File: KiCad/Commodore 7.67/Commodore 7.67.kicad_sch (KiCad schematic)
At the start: 22 parts, among them U1 SX1281IMLTRT, U2 SN65HVD74DR, U3 LPF-B0R3, Y1 52MHz

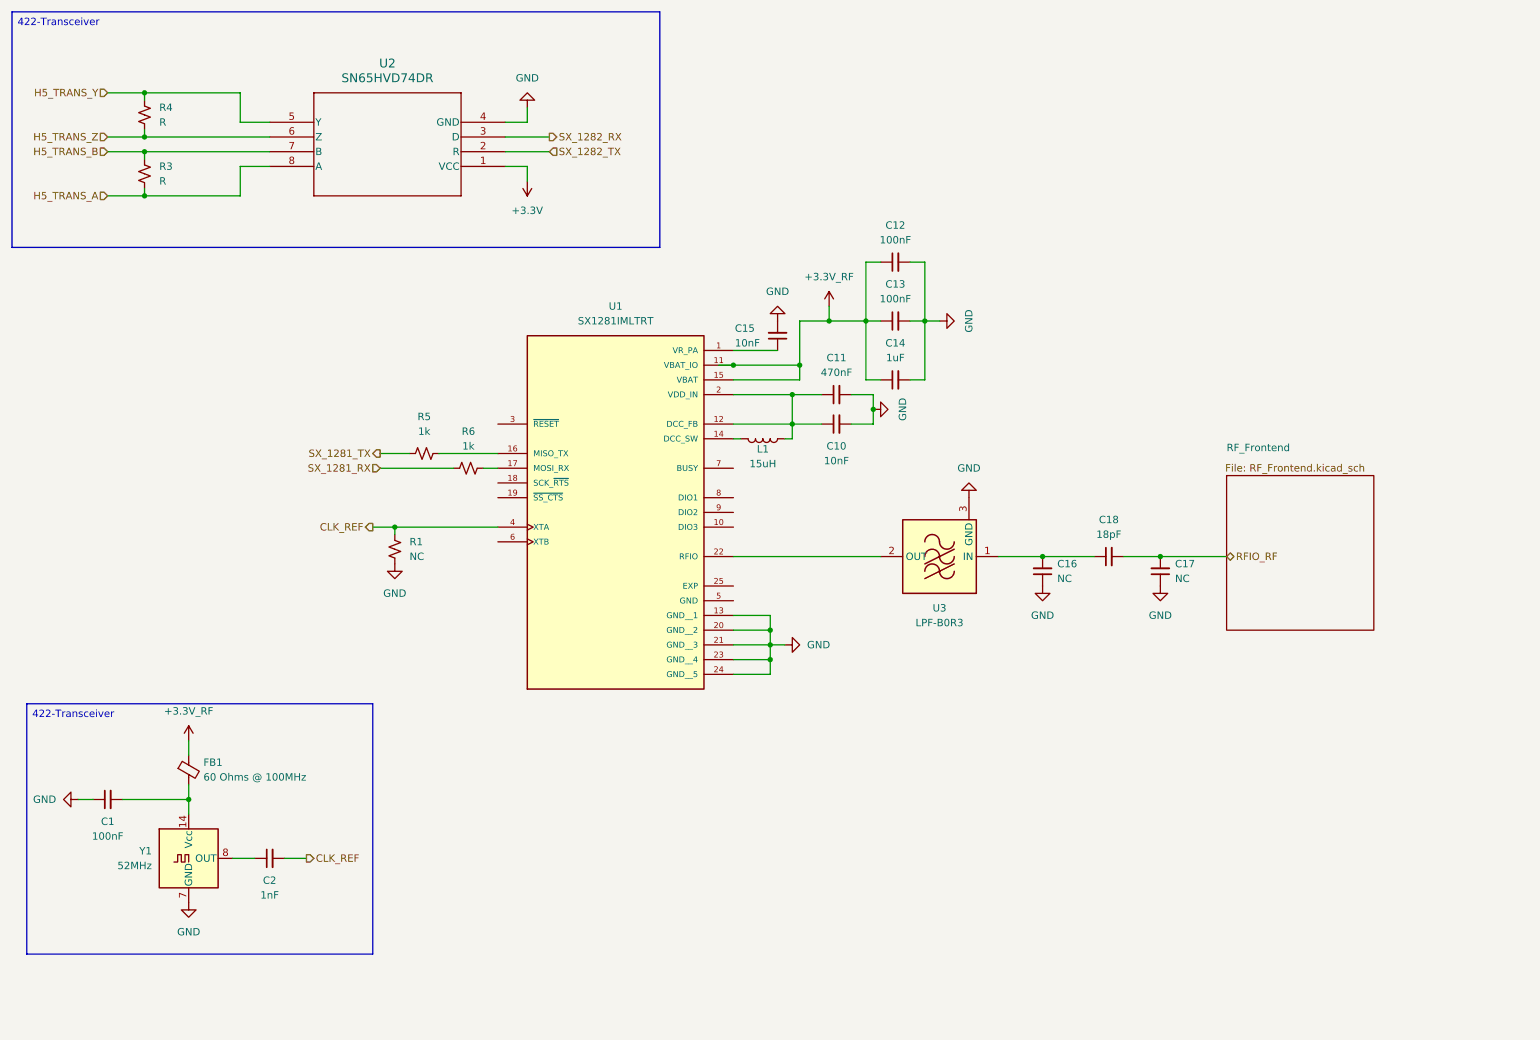
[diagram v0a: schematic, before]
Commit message: ts updates for ts sx1281
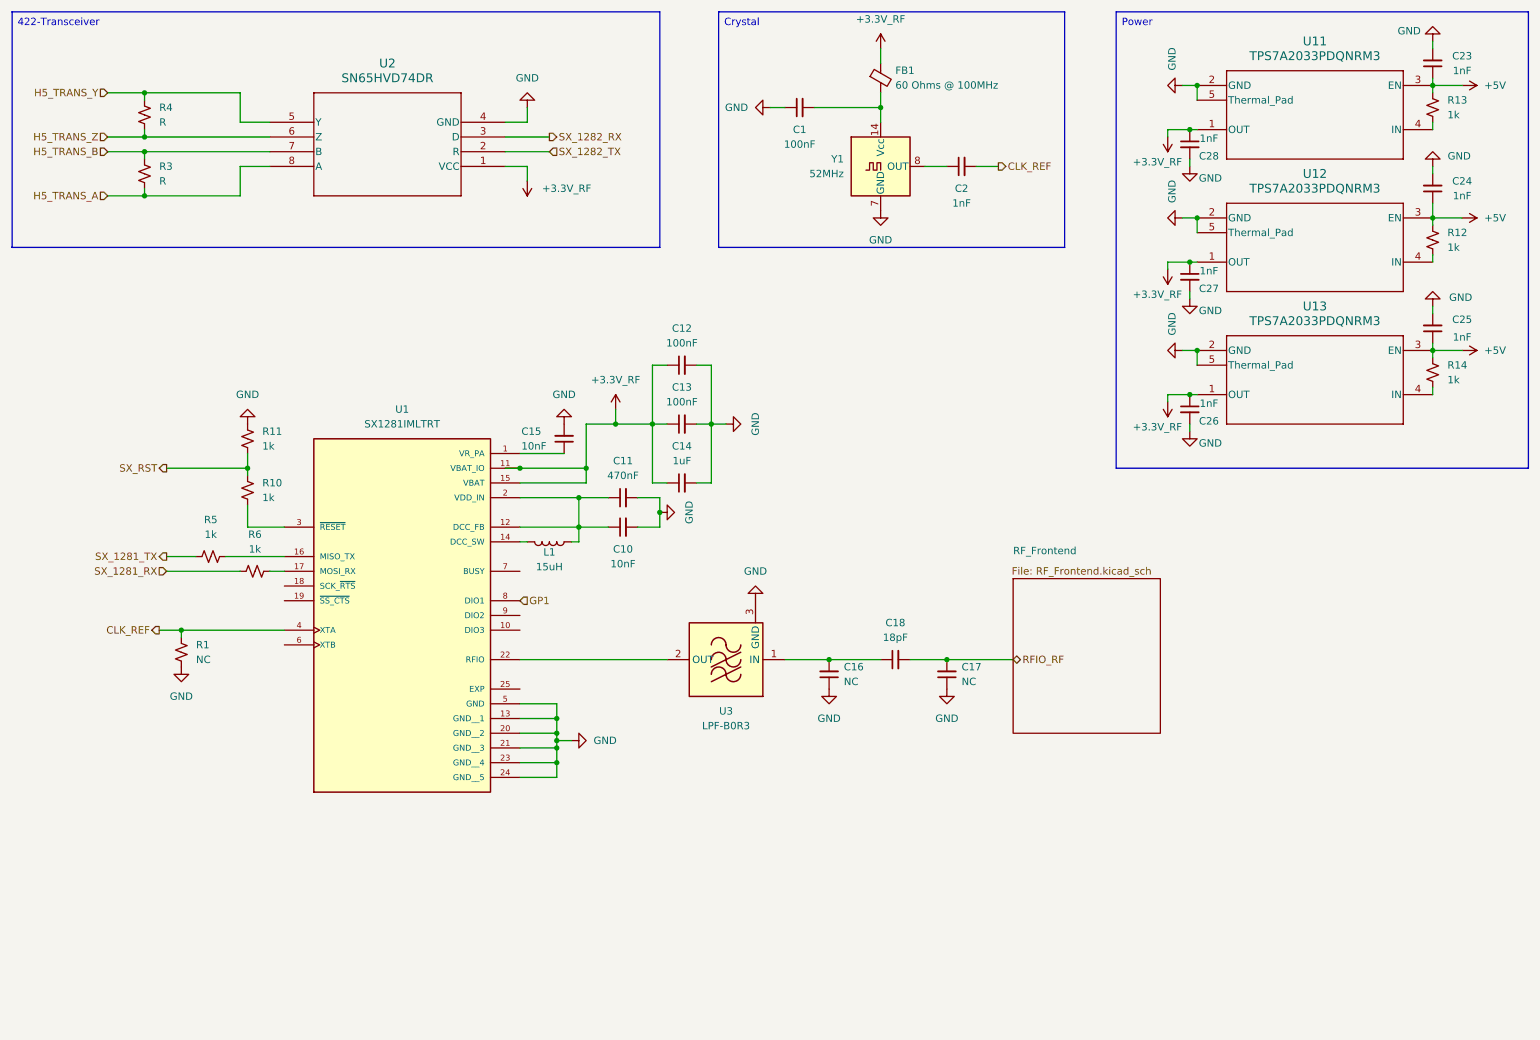
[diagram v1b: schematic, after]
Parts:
- added C23, C24, C25, C26, C27, C28: 1nF, symbol Device:C_Small
- added R10, R11, R12, R13, R14: 1k, symbol Device:R_Small_US
- added U11, U12, U13: TPS7A2033PDQNRM3, DQN0004A-MFG, symbol 2025-10-22_05-18-30:TPS7A2033PDQNRM3
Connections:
- net +3.3V is gone; now on net +3.3V_RF: U2.1 (VCC)
- net +3.3V_RF: now also C26.1, C27.1, C28.1, U11.1 (OUT), U12.1 (OUT), U13.1 (OUT)
- net GND: now also U1.5 (GND), C23.2, C24.2, C25.2, C26.2, C27.2, C28.2, R11.2, U11.2 (GND), U11.5 (Thermal_Pad), U12.2 (GND), U12.5 (Thermal_Pad), U13.2 (GND), U13.5 (Thermal_Pad)
- net at U1.3 (~{RESET}): now also R10.1
- net GP1: now reaches U1.8 (DIO1)
- new net: R12.1, U12.4 (IN)
- new net: R14.1, U13.4 (IN)
- new net: R13.1, U11.4 (IN)
- new net +5V: C23.1, C24.1, C25.1, R12.2, R13.2, R14.2, U11.3 (EN), U12.3 (EN), U13.3 (EN)
- new net SX_RST: R10.2, R11.1
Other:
- moved on the sheet: C1, C10, C11, C12, C13, C14, C15, C16, C17, C18, C2, FB1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

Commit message: radio development
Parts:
- removed C1, C12, C13: 100nF, symbol Device:C_Small
- removed C10, C15: 10nF, symbol Device:C_Small
- removed C11: 470nF, symbol Device:C_Small
- removed C14: 1uF, symbol Device:C_Small
- removed C16, C17: NC, symbol Device:C_Small
- removed C18: 18pF, symbol Device:C_Small
- removed C2, C23, C24, C25, C26, C27, C28: 1nF, symbol Device:C_Small
- removed FB1: 60 Ohms @ 100MHz, symbol Device:FerriteBead_Small
- removed L1: 15uH, symbol Device:L
- removed R1: NC, symbol Device:R_Small_US
- removed R10, R11, R12, R13, R14, R5, R6: 1k, symbol Device:R_Small_US
- removed R3, R4: R, symbol Device:R_Small_US
- removed U1: SX1281IMLTRT, SX1281IMLTRT:XCVR_SX1281IMLTRT, symbol SX1281IMLTRT:SX1281IMLTRT
- removed U11, U12, U13: TPS7A2033PDQNRM3, DQN0004A-MFG, symbol 2025-10-22_05-18-30:TPS7A2033PDQNRM3
- removed U2: SN65HVD74DR, D8_TEX, symbol 2025-10-21_21-34-58:SN65HVD74DR
- removed U3: LPF-B0R3, RF_Mini-Circuits:Mini-Circuits_HZ1198_LandPatternPL-247, symbol RF_Filter:LPF-B0R3
- removed Y1: 52MHz, Oscillator:Oscillator_DIP-14, symbol Oscillator:TCXO-14
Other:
- added sheet Crystal (Crystal.kicad_sch)
- added sheet Power (Power.kicad_sch)
- added sheet SX1281 (SX1281.kicad_sch)
- added sheet Transceiver (Transceiver.kicad_sch)

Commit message: yay done
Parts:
- added J3: B6B-XH-A, B6B-XH-A:JST_B6B-XH-A, symbol B6B-XH-A:B6B-XH-A
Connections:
- new net GND: J3.1
- new net SX_CS: J3.3
- new net SX_MISO: J3.6
- new net SX_MOSI: J3.5
- new net SX_SCK: J3.4
- new net VBATT: J3.2
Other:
- removed sheet Transceiver

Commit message: its over
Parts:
- renumbered J3 to J1
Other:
- sheet RF_Frontend renamed 2_4GHz_Frontend
- added sheet 1_2GHz_Frontend (1_2GHz_Frontend.kicad_sch)
- added sheet SX1781 (SX1781.kicad_sch)
- sheet 2_4GHz_Frontend: file RF_Frontend.kicad_sch -> 2_4GHz_Frontend.kicad_sch
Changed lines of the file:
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@@
 	(wire
 		(pts
-			(xy 111.76 39.37) (xy 111.76 67.31)
-		)
-		(stroke
-			(width 0)
-			(type default)
-		)
-	)
-	(wire
-		(pts
-			(xy 127 106.68) (xy 123.19 106.68)
-		)
-		(stroke
-			(width 0)
-			(type default)
-		)
-	)
-	(wire
-		(pts
-			(xy 123.19 76.2) (xy 166.37 76.2)
-		)
-		(stroke
-			(width 0)
-			(type default)
-		)
-	)
-	(wire
-		(pts
-			(xy 104.14 54.61) (xy 102.87 54.61)
-		)
-		(stroke
-			(width 0)
-			(type default)
-		)
-	)
-	(wire
-		(pts
-			(xy 106.68 39.37) (xy 106.68 55.88)
-		)
-		(stroke
-			(width 0)
-			(type default)
-		)
-	)
-	(wire
-		(pts
-			(xy 109.22 39.37) (xy 109.22 67.31)
+			(xy 185.42 95.25) (xy 106.68 95.25)
+		)
+		(stroke
+			(width 0)
+			(type default)
+		)
+	)
+	(wire
+		(pts
+			(xy 224.79 73.66) (xy 224.79 77.47)
+		)
+		(stroke
+			(width 0)
+			(type default)
+		)
+	)
+	(wire
+		(pts
+			(xy 185.42 91.44) (xy 109.22 91.44)
+		)
+		(stroke
+			(width 0)
+			(type default)
+		)
+	)
+	(wire
+		(pts
+			(xy 194.31 77.47) (xy 194.31 68.58)
 		)
 		(stroke
@@
 	(wire
 		(pts
-			(xy 104.14 39.37) (xy 104.14 54.61)
-		)
-		(stroke
-			(width 0)
-			(type default)
-		)
-	)
-	(wire
-		(pts
-			(xy 106.68 55.88) (xy 105.41 55.88)
-		)
-		(stroke
-			(width 0)
-			(type default)
-		)
-	)
-	(wire
-		(pts
-			(xy 123.19 71.12) (xy 166.37 71.12)
-		)
-		(stroke
-			(width 0)
-			(type default)
-		)
-	)
-	(wire
-		(pts
-			(xy 123.19 88.9) (xy 127 88.9)
-		)
-		(stroke
-			(width 0)
-			(type default)
-		)
-	)
-	(wire
-		(pts
-			(xy 105.41 55.88) (xy 105.41 67.31)
+			(xy 104.14 39.37) (xy 104.14 97.79)
+		)
+		(stroke
+			(width 0)
+			(type default)
+		)
+	)
+	(wire
+		(pts
+			(xy 106.68 39.37) (xy 106.68 95.25)
+		)
+		(stroke
+			(width 0)
+			(type default)
+		)
+	)
+	(wire
+		(pts
+			(xy 189.23 77.47) (xy 189.23 68.58)
+		)
+		(stroke
+			(width 0)
+			(type default)
+		)
+	)
+	(wire
+		(pts
+			(xy 207.01 77.47) (xy 207.01 73.66)
+		)
+		(stroke
+			(width 0)
+			(type default)
+		)
+	)
+	(wire
+		(pts
+			(xy 109.22 91.44) (xy 109.22 39.37)
+		)
+		(stroke
+			(width 0)
+			(type default)
+		)
+	)
+	(wire
+		(pts
+			(xy 185.42 97.79) (xy 104.14 97.79)
 		)
 		(stroke
@@
 	(wire
 		(pts
-			(xy 102.87 54.61) (xy 102.87 67.31)
-		)
-		(stroke
-			(width 0)
-			(type default)
-		)
-	)
-	(wire
-		(pts
-			(xy 127 88.9) (xy 127 106.68)
+			(xy 111.76 88.9) (xy 111.76 39.37)
+		)
+		(stroke
+			(width 0)
+			(type default)
+		)
+	)
+	(wire
+		(pts
+			(xy 185.42 88.9) (xy 111.76 88.9)
+		)
+		(stroke
+			(width 0)
+			(type default)
+		)
+	)
+	(wire
+		(pts
+			(xy 207.01 73.66) (xy 224.79 73.66)
 		)
 		(stroke
@@
 	(hierarchical_label "SX_MOSI"
 		(shape output)
-		(at 109.22 67.31 270)
-		(effects
-			(font
-				(size 1.27 1.27)
-			)
-			(justify right)
+		(at 185.42 91.44 0)
+		(effects
+			(font
+				(size 1.27 1.27)
+			)
+			(justify left)
 		)
 	)
 	(hierarchical_label "SX_MISO"
 		(shape input)
-		(at 111.76 67.31 270)
-		(effects
-			(font
-				(size 1.27 1.27)
-			)
-			(justify right)
+		(at 185.42 88.9 0)
+		(effects
+			(font
+				(size 1.27 1.27)
+			)
+			(justify left)
 		)
 	)
 	(hierarchical_label "GP1"
 		(shape input)
-		(at 166.37 76.2 0)
+		(at 194.31 68.58 90)
 		(effects
 			(font
@@
 	(hierarchical_label "CLK_REF"
 		(shape output)
-		(at 123.19 106.68 180)
+		(at 224.79 77.47 270)
 		(effects
 			(font
@@
 	(hierarchical_label "SX_CS"
 		(shape input)
-		(at 102.87 67.31 270)
-		(effects
-			(font
-				(size 1.27 1.27)
-			)
-			(justify right)
+		(at 185.42 97.79 0)
+		(effects
+			(font
+				(size 1.27 1.27)
+			)
+			(justify left)
 		)
 	)
 	(hierarchical_label "RFIO_RF"
 		(shape bidirectional)
-		(at 123.19 71.12 180)
+		(at 189.23 77.47 270)
 		(effects
 			(font
@@
 	(hierarchical_label "RFIO_RF"
 		(shape bidirectional)
-		(at 166.37 71.12 0)
+		(at 189.23 68.58 90)
 		(effects
 			(font
@@
 	(hierarchical_label "GP1"
 		(shape input)
-		(at 123.19 76.2 180)
+		(at 194.31 77.47 270)
 		(effects
 			(font
@@
 	(hierarchical_label "CLK_REF"
 		(shape output)
-		(at 123.19 88.9 180)
+		(at 207.01 77.47 270)
 		(effects
 			(font
@@
 	(hierarchical_label "SX_SCK"
 		(shape input)
-		(at 105.41 67.31 270)
-		(effects
-			(font
-				(size 1.27 1.27)
-			)
-			(justify right)
+		(at 185.42 95.25 0)
+		(effects
+			(font
+				(size 1.27 1.27)
+			)
+			(justify left)
 		)
 	)
@@
 		(dnp no)
 		(fields_autoplaced yes)
-		(property "Reference" "J3"
+		(property "Reference" "J1"
 			(at 115.57 30.4799 90)
 			(effects
@@
 			(project ""
 				(path "/92fa3f49-0e94-4664-860a-d244369fb976"
-					(reference "J3")
+					(reference "J1")
 					(unit 1)
 				)
@@
 	)
 	(sheet
-		(at 95.25 101.6)
-		(size 27.94 15.24)
+		(at 219.71 77.47)
+		(size 15.24 27.94)
 		(exclude_from_sim no)
 		(in_bom yes)
@@
 		)
 		(property "Sheetname" "Crystal"
-			(at 95.25 100.8884 0)
+			(at 219.71 76.7584 0)
 			(effects
 				(font
@@
 		)
 		(property "Sheetfile" "Crystal.kicad_sch"
-			(at 95.25 117.4246 0)
+			(at 219.71 105.9946 0)
 			(effects
 				(font
@@
 	)
 	(sheet
-		(at 166.37 58.42)
-		(size 106.68 100.33)
+		(at 176.53 25.4)
+		(size 100.33 43.18)
 		(exclude_from_sim no)
 		(in_bom yes)
@@
 			(color 0 0 0 0.0000)
 		)
-		(property "Sheetname" "RF_Frontend"
-			(at 166.37 54.356 0)
+		(property "Sheetname" "2_4GHz_Frontend"
+			(at 176.53 21.336 0)
 			(effects
 				(font
@@
 			)
 		)
-		(property "Sheetfile" "RF_Frontend.kicad_sch"
-			(at 166.116 56.388 0)
+		(property "Sheetfile" "2_4GHz_Frontend.kicad_sch"
+			(at 176.276 23.368 0)
 			(effects
 				(font
@@
 	)
 	(sheet
-		(at 80.01 67.31)
-		(size 43.18 24.13)
+		(at 16.51 148.59)
+		(size 140.97 41.91)
 		(exclude_from_sim no)
 		(in_bom yes)
@@
 			(color 0 0 0 0.0000)
 		)
+		(property "Sheetname" "1_2GHz_Frontend"
+			(at 16.51 147.8784 0)
+			(effects
+				(font
+					(size 1.27 1.27)
+				)
+				(justify left bottom)
+			)
+		)
+		(property "Sheetfile" "1_2GHz_Frontend.kicad_sch"
+			(at 16.51 191.0846 0)
+			(effects
+				(font
+					(size 1.27 1.27)
+				)
+				(justify left top)
+			)
+		)
+		(instances
+			(project "Commodore 7.67"
+				(path "/92fa3f49-0e94-4664-860a-d244369fb976"
+					(page "8")
+				)
+			)
+		)
+	)
+	(sheet
+		(at 64.135 111.125)
+		(size 52.07 33.02)
+		(exclude_from_sim no)
+		(in_bom yes)
+		(on_board yes)
+		(dnp no)
+		(fields_autoplaced yes)
+		(stroke
+			(width 0.1524)
+			(type solid)
+		)
+		(fill
+			(color 0 0 0 0.0000)
+		)
+		(property "Sheetname" "SX1781"
+			(at 64.135 110.4134 0)
+			(effects
+				(font
+					(size 1.27 1.27)
+				)
+				(justify left bottom)
+			)
+		)
+		(property "Sheetfile" "SX1781.kicad_sch"
+			(at 64.135 144.7296 0)
+			(effects
+				(font
+					(size 1.27 1.27)
+				)
+				(justify left top)
+			)
+		)
+		(instances
+			(project "Commodore 7.67"
+				(path "/92fa3f49-0e94-4664-860a-d244369fb976"
+					(page "7")
+				)
+			)
+		)
+	)
+	(sheet
+		(at 185.42 77.47)
+		(size 24.13 43.18)
+		(exclude_from_sim no)
+		(in_bom yes)
+		(on_board yes)
+		(dnp no)
+		(fields_autoplaced yes)
+		(stroke
+			(width 0.1524)
+			(type solid)
+		)
+		(fill
+			(color 0 0 0 0.0000)
+		)
 		(property "Sheetname" "SX1281"
-			(at 80.01 66.5984 0)
+			(at 185.42 76.7584 0)
 			(effects
 				(font
@@
 		)
 		(property "Sheetfile" "SX1281.kicad_sch"
-			(at 80.01 92.0246 0)
-			(effects
-				(font
+			(at 185.42 121.2346 0)
+			(effects
+				(font
